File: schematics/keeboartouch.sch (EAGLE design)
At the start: 56 parts, among them K1 TOUCHKEY, K10 TOUCHKEY, K11 TOUCHKEY, K12 TOUCHKEY, K13 TOUCHKEY, K14 TOUCHKEY, K15 TOUCHKEY, K16 TOUCHKEY, K17 TOUCHKEY, K18 TOUCHKEY, K19 TOUCHKEY, K2 TOUCHKEY, K20 TOUCHKEY, K21 TOUCHKEY, K22 TOUCHKEY, K23 TOUCHKEY, K24 TOUCHKEY, K25 TOUCHKEY, K26 TOUCHKEY, K27 TOUCHKEY, K28 TOUCHKEY, K29 TOUCHKEY, K3 TOUCHKEY, K30 TOUCHKEY, K31 TOUCHKEY, K32 TOUCHKEY, K33 TOUCHKEY, K34 TOUCHKEY, K35 TOUCHKEY, K36 TOUCHKEY, K37 TOUCHKEY, K38 TOUCHKEY, K39 TOUCHKEY, K4 TOUCHKEY, K40 TOUCHKEY, K5 TOUCHKEY, K6 TOUCHKEY, K7 TOUCHKEY, K8 TOUCHKEY, K9 TOUCHKEY, U2 PRO_MICROSMD

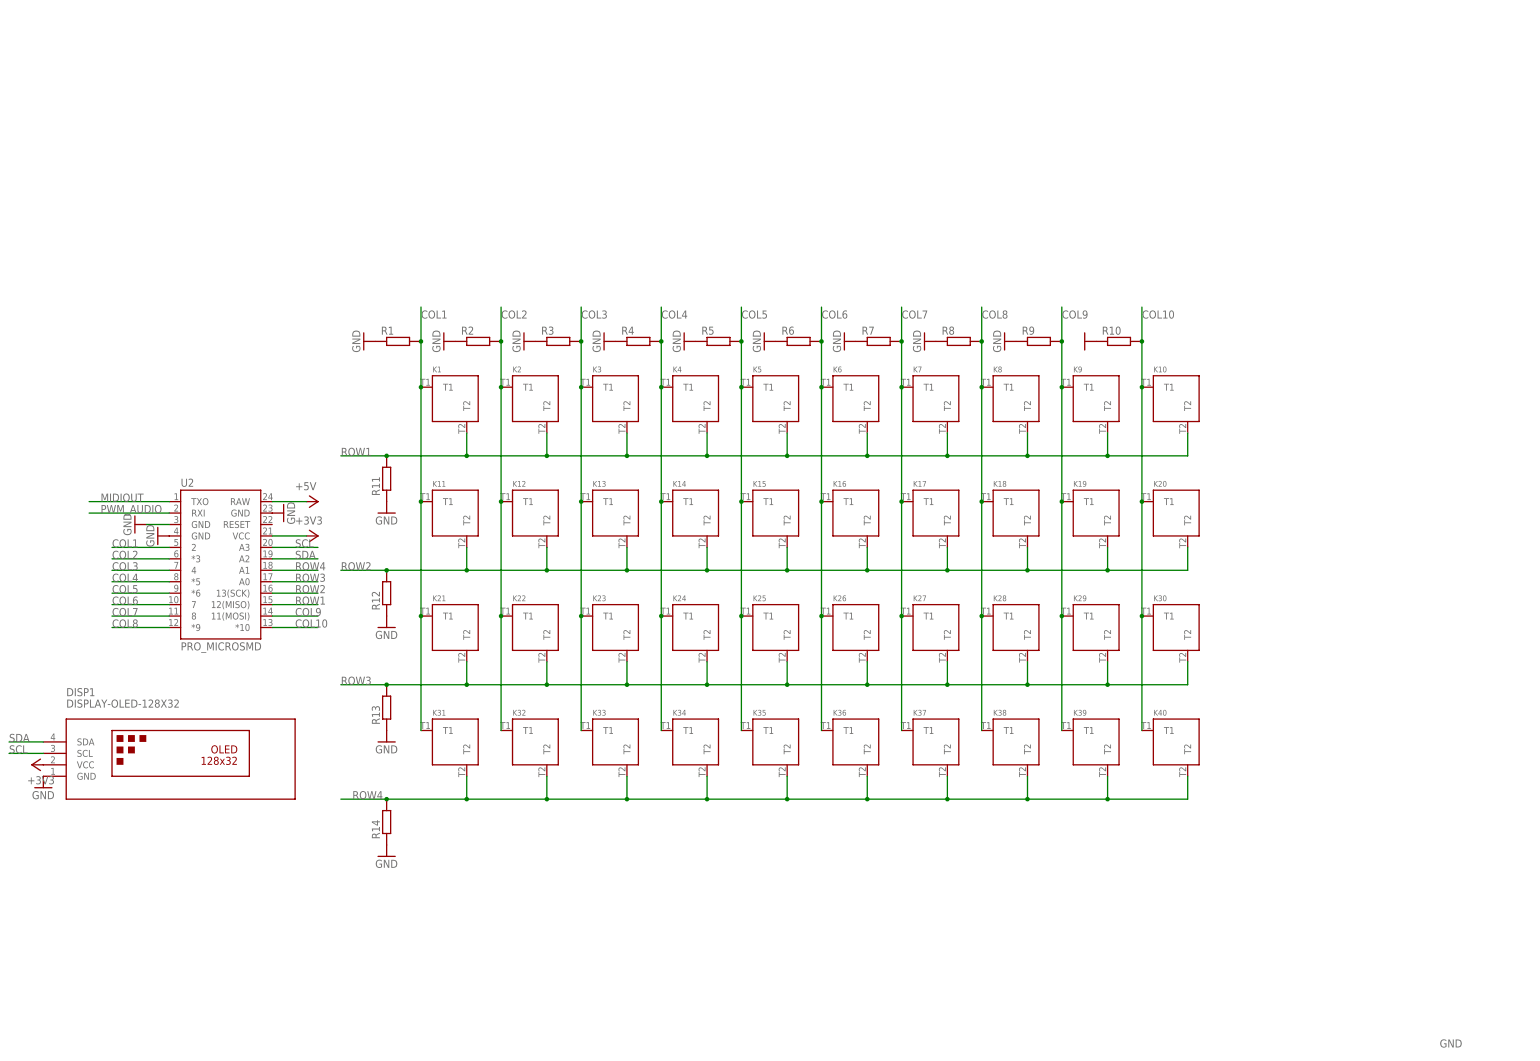
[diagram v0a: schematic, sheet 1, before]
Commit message: four mount holes thx to jp
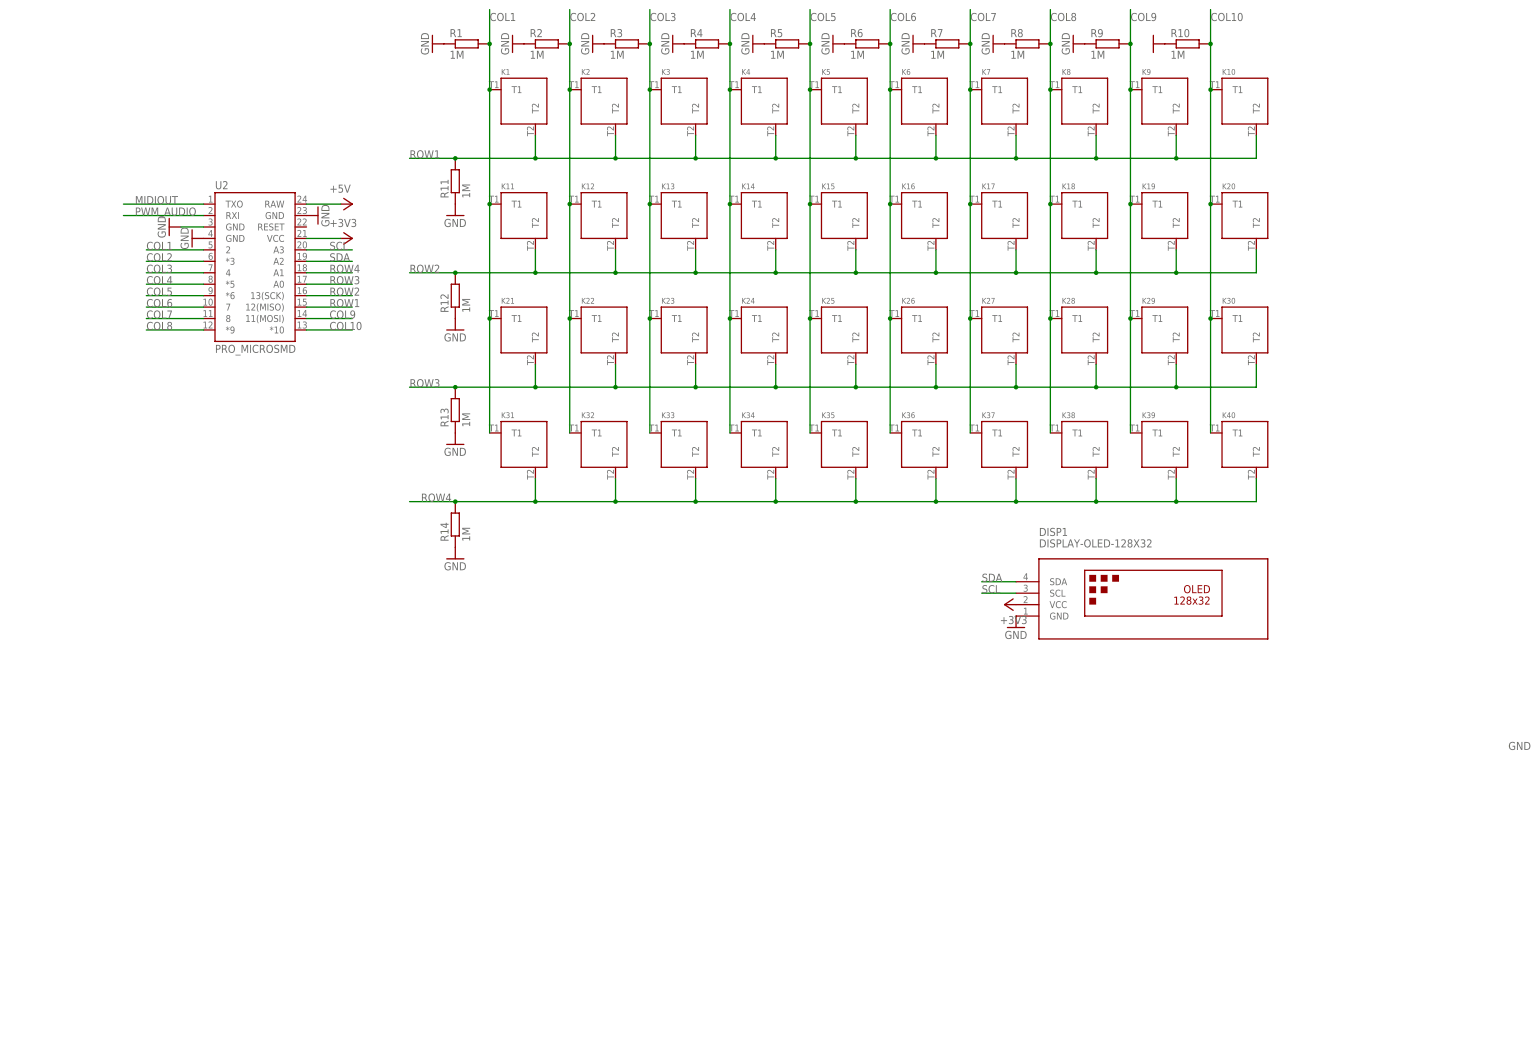
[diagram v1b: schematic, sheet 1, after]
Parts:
- R1, R10, R11, R12, R13, R14, R2, R3, R4, R5, R6, R7, R8, R9: value (none) -> 1M
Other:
- moved on the sheet: DISP1, K1, K10, K11, K12, K13, K14, K15, K16, K17, K18, K19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

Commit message: now with silly topsilk
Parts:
- removed DISP1: DISPLAY-OLED-128X32, diy-modules:DISPLAY-OLED-128X32
- added J1: (no value), SparkFun-Connectors:CONN_04
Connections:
- net +3V3: now also J1.2; no longer DISP1.VCC
- net GND: now also J1.1; no longer DISP1.GND
- net SCL: now also J1.3; no longer DISP1.SCL
- net SDA: now also J1.4; no longer DISP1.SDA
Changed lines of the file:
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@@
 <part name="R14" library="rcl" library_urn="urn:adsk.eagle:library:334" deviceset="R-EU_" device="R0805" package3d_urn="urn:adsk.eagle:package:23553/2" value="1M"/>
 <part name="GND17" library="supply1" library_urn="urn:adsk.eagle:library:371" deviceset="GND" device=""/>
-<part name="DISP1" library="diy-modules" deviceset="DISPLAY-OLED-128X32" device=""/>
 <part name="GND18" library="supply1" library_urn="urn:adsk.eagle:library:371" deviceset="GND" device=""/>
 <part name="+3V2" library="supply1" library_urn="urn:adsk.eagle:library:371" deviceset="+3V3" device=""/>
 <part name="FRAME1" library="frames" library_urn="urn:adsk.eagle:library:229" deviceset="FRAME_A_L" device=""/>
+<part name="J1" library="SparkFun-Connectors" library_urn="urn:adsk.eagle:library:513" deviceset="CONN_04" device="" package3d_urn="urn:adsk.eagle:package:38085/1"/>
 </parts>
 <sheets>
@@
 <attribute name="VALUE" x="81.28" y="68.58" size="1.778" layer="96"/>
 </instance>
-<instance part="DISP1" gate="G$1" x="238.76" y="63.5" smashed="yes">
-<attribute name="NAME" x="213.36" y="76.2" size="1.778" layer="95"/>
-<attribute name="VALUE" x="213.36" y="73.66" size="1.778" layer="96"/>
-</instance>
 <instance part="GND18" gate="1" x="208.28" y="55.88" smashed="yes">
 <attribute name="VALUE" x="205.74" y="53.34" size="1.778" layer="96"/>
 </instance>
-<instance part="+3V2" gate="G$1" x="205.74" y="60.96" smashed="yes" rot="R90">
-<attribute name="VALUE" x="210.82" y="58.42" size="1.778" layer="96" rot="R180"/>
+<instance part="+3V2" gate="G$1" x="203.2" y="60.96" smashed="yes" rot="R90">
+<attribute name="VALUE" x="203.2" y="60.96" size="1.778" layer="96" rot="R180"/>
 </instance>
 <instance part="FRAME1" gate="G$1" x="0" y="0" smashed="yes"/>
@@
 <attribute name="SHEET" x="259.08" y="1.27" size="2.54" layer="94"/>
 <attribute name="DRAWING_NAME" x="190.5" y="19.05" size="2.54" layer="94"/>
+</instance>
+<instance part="J1" gate="G$1" x="213.36" y="60.96" smashed="yes" rot="MR0">
+<attribute name="VALUE" x="218.44" y="53.594" size="1.778" layer="96" font="vector" rot="MR0"/>
+<attribute name="NAME" x="218.44" y="69.088" size="1.778" layer="95" font="vector" rot="MR0"/>
 </instance>
 </instances>
@@
 </segment>
 <segment>
-<pinref part="DISP1" gate="G$1" pin="GND"/>
 <pinref part="GND18" gate="1" pin="GND"/>
+<pinref part="J1" gate="G$1" pin="1"/>
+<pinref part="J1" gate="G$1" pin="1"/>
 </segment>
 </net>
@@
 </segment>
 <segment>
-<pinref part="DISP1" gate="G$1" pin="VCC"/>
 <pinref part="+3V2" gate="G$1" pin="+3V3"/>
+<pinref part="J1" gate="G$1" pin="2"/>
+<pinref part="J1" gate="G$1" pin="2"/>
+<wire x1="205.74" y1="60.96" x2="208.28" y2="60.96" width="0.1524" layer="91"/>
 </segment>
 </net>
@@
 </segment>
 <segment>
-<pinref part="DISP1" gate="G$1" pin="SCL"/>
 <wire x1="208.28" y1="63.5" x2="200.66" y2="63.5" width="0.1524" layer="91"/>
 <label x="200.66" y="63.5" size="1.778" layer="95"/>
+<pinref part="J1" gate="G$1" pin="3"/>
 </segment>
 </net>
@@
 </segment>
 <segment>
-<pinref part="DISP1" gate="G$1" pin="SDA"/>
 <wire x1="208.28" y1="66.04" x2="200.66" y2="66.04" width="0.1524" layer="91"/>
 <label x="200.66" y="66.04" size="1.778" layer="95"/>
-</segment>
-</net>
+<pinref part="J1" gate="G$1" pin="4"/>
+</segment>
+</net>
